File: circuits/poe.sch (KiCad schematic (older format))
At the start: 19 parts, among them U11 Si3402-B-GM(QFN-20_5x5mm)

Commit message: finished schematic corrections, working on layout
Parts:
- removed C11: C_100nF_1206, Capacitor_SMD:C_1206_3216Metric_Pad1.33x1.80mm_HandSolder, symbol Open_Automation:C_100nF_1206
- removed C12, C13: C_1uF_1206, Capacitor_SMD:C_1206_3216Metric_Pad1.33x1.80mm_HandSolder, symbol Open_Automation:C_1uF_1206
- removed C14: C_1nF_0402, Capacitor_SMD:C_0402_1005Metric_Pad0.74x0.62mm_HandSolder, symbol Open_Automation:C_1nF_0402
- removed C15: C_100nF_0402, Capacitor_SMD:C_0402_1005Metric_Pad0.74x0.62mm_HandSolder, symbol Open_Automation:C_100nF_0402
- removed C16: C_15uF, Capacitor_THT:CP_Radial_D6.3mm_P2.50mm, symbol Open_Automation:C_15uF
- removed C17: C_680uF, Capacitor_THT:CP_Radial_D6.3mm_P2.50mm, symbol Open_Automation:C_680uF
- removed C18: C_22uF_0805, Capacitor_SMD:C_0805_2012Metric_Pad1.18x1.45mm_HandSolder, symbol Open_Automation:C_22uF_0805
- removed D7: SS510, Diode_SMD:D_SMC_Handsoldering, symbol Open_Automation:SS510
- removed L1: L_33uH, Inductor_SMD:L_12x12mm_H6mm, symbol Open_Automation:L_33uH
- removed L2: FB, Inductor_SMD:L_1206_3216Metric, symbol Open_Automation:FB
- removed R46: R_47K_0402, Resistor_SMD:R_0402_1005Metric_Pad0.72x0.64mm_HandSolder, symbol Open_Automation:R_47K_0402
- removed R47: R_49.9_0402, Resistor_SMD:R_0402_1005Metric_Pad0.72x0.64mm_HandSolder, symbol Open_Automation:R_49.9_0402
- removed R48: R_25K5, Resistor_SMD:R_0603_1608Metric_Pad0.98x0.95mm_HandSolder, symbol Open_Automation:R_25K5
- removed R49: R_1K_0402, Resistor_SMD:R_0402_1005Metric_Pad0.72x0.64mm_HandSolder, symbol Open_Automation:R_1K_0402
- removed R50: R_8K2_0402, Resistor_SMD:R_0402_1005Metric_Pad0.72x0.64mm_HandSolder, symbol Open_Automation:R_8K2_0402
- removed SJ1, SJ2: SJ, Open_Automation:SJUMP, symbol Open_Automation:SJ
- removed U11: Si3402-B-GM(QFN-20_5x5mm), Open_Automation:QFN-20_5x5mm(Si3402-B-GM), symbol ESP32-PoE_Rev_E:Si3402-B-GM(QFN-20_5x5mm)
- added C11: C_2.2nF, Capacitor_SMD:C_1206_3216Metric_Pad1.33x1.80mm_HandSolder, symbol Open_Automation:C_2.2nF
- added C12: C_100nF_1206, Capacitor_SMD:C_1206_3216Metric_Pad1.33x1.80mm_HandSolder, symbol Open_Automation:C_100nF_1206
- added C13: C_0.1uF, Capacitor_SMD:C_0603_1608Metric_Pad1.08x0.95mm_HandSolder, symbol Open_Automation:C_0.1uF
- added C14: C_10nF, Capacitor_SMD:C_1206_3216Metric_Pad1.33x1.80mm_HandSolder, symbol Open_Automation:C_10nF
- added C15: C_47nF, Capacitor_SMD:C_0603_1608Metric_Pad1.08x0.95mm_HandSolder, symbol Open_Automation:C_47nF
- added C16: C_22uF_63V, Capacitor_SMD:C_Elec_6.3x7.7, symbol Open_Automation:C_22uF_63V
- added C17: C_220nF, Capacitor_SMD:C_1206_3216Metric_Pad1.33x1.80mm_HandSolder, symbol Open_Automation:C_220nF
- added C18: C_1uF_1206, Capacitor_SMD:C_1206_3216Metric_Pad1.33x1.80mm_HandSolder, symbol Open_Automation:C_1uF_1206
- added C19: C_10uF_Ta, Capacitor_Tantalum_SMD:CP_EIA-6032-15_Kemet-U_Pad2.25x2.35mm_HandSolder, symbol Open_Automation:C_10uF_Ta
- added C20: C_1uF, Capacitor_SMD:C_0603_1608Metric_Pad1.08x0.95mm_HandSolder, symbol Open_Automation:C_1uF
- added C21: C_47uF_Al, Capacitor_SMD:CP_Elec_6.3x7.7, symbol Open_Automation:C_47uF_Al
- added C22: C_100pF, Capacitor_SMD:C_0402_1005Metric_Pad0.74x0.62mm_HandSolder, symbol Open_Automation:C_100pF
- added C23: C_6.8nF, Capacitor_SMD:C_0402_1005Metric_Pad0.74x0.62mm_HandSolder, symbol Open_Automation:C_6.8nF
- added C24: C_47uF_Ta, Capacitor_Tantalum_SMD:CP_EIA-6032-15_Kemet-U_Pad2.25x2.35mm_HandSolder, symbol Open_Automation:C_47uF_Ta
- added C25: C_47uF, Capacitor_SMD:C_1210_3225Metric_Pad1.33x2.70mm_HandSolder, symbol Open_Automation:C_47uF
- added D10, D9: D_Bridge_+-AA, Open_Automation:Diode_Bridge_HD01, symbol Open_Automation:D_Bridge_+-AA
- added D11: D_SMAJ58A, Diode_SMD:D_SMA_Handsoldering, symbol Open_Automation:D_SMAJ58A
- added D12, D8: D_MURA120, Diode_SMD:D_SMA_Handsoldering, symbol Open_Automation:D_MURA120
- added D13, D14: BAS16, Package_TO_SOT_SMD:SOT-23, symbol Open_Automation:BAS16
- added D15: D_MBRS540T3G, Diode_SMD:D_SMC_Handsoldering, symbol Open_Automation:D_MBRS540T3G
- added J20: Conn_02x02_Counter_Clockwise, Connector_PinHeader_2.54mm:PinHeader_2x02_P2.54mm_Vertical_SMD, symbol Connector_Generic:Conn_02x02_Counter_Clockwise
- added L1: L_4.7uH, Open_Automation:L_5.4x5.3_H3, symbol Open_Automation:L_4.7uH
- added Q8: Q_FDC2512, Package_TO_SOT_SMD:SOT-23-6_Handsoldering, symbol Open_Automation:Q_FDC2512
- added R47: R_3.01K, Resistor_SMD:R_0603_1608Metric_Pad0.98x0.95mm_HandSolder, symbol Open_Automation:R_3.01K
- added R48: R_69.8K, Resistor_SMD:R_0603_1608Metric_Pad0.98x0.95mm_HandSolder, symbol Open_Automation:R_69.8K
- added R49: R_24.9K, Resistor_SMD:R_0603_1608Metric_Pad0.98x0.95mm_HandSolder, symbol Open_Automation:R_24.9K
- added R50: R_63.4, Resistor_SMD:R_0603_1608Metric_Pad0.98x0.95mm_HandSolder, symbol Open_Automation:R_63.4
- added R51: R_80.6K, Resistor_SMD:R_0402_1005Metric_Pad0.72x0.64mm_HandSolder, symbol Open_Automation:R_80.6K
- added R52: R_59K, Resistor_SMD:R_0402_1005Metric_Pad0.72x0.64mm_HandSolder, symbol Open_Automation:R_59K
- added R53, R60: R_49.9_0402, Resistor_SMD:R_0402_1005Metric_Pad0.72x0.64mm_HandSolder, symbol Open_Automation:R_49.9_0402
- added R54: R_49.9K, Resistor_SMD:R_0402_1005Metric_Pad0.72x0.64mm_HandSolder, symbol Open_Automation:R_49.9K
- added R55: R_0.56, Resistor_SMD:R_0603_1608Metric_Pad0.98x0.95mm_HandSolder, symbol Open_Automation:R_0.56
- added R56, R58: R_402, Resistor_SMD:R_0402_1005Metric_Pad0.72x0.64mm_HandSolder, symbol Open_Automation:R_402
- added R57: R_2K, Resistor_SMD:R_0402_1005Metric_Pad0.72x0.64mm_HandSolder, symbol Open_Automation:R_2K
- added R59: R_10K_0402, Resistor_SMD:R_0402_1005Metric_Pad0.72x0.64mm_HandSolder, symbol Open_Automation:R_10K_0402
- added R61: R_7.15K, Resistor_SMD:R_0402_1005Metric_Pad0.72x0.64mm_HandSolder, symbol Open_Automation:R_7.15K
- added R62: R_41.2K, Resistor_SMD:R_0402_1005Metric_Pad0.72x0.64mm_HandSolder, symbol Open_Automation:R_41.2K
- added R63: R_13.3K, Resistor_SMD:R_0402_1005Metric_Pad0.72x0.64mm_HandSolder, symbol Open_Automation:R_13.3K
- added TR1: TPS23754-TRANSFORMER, Open_Automation:TPS23754, symbol Open_Automation:TPS23754-TRANSFORMER
- added U11: TPS23754PWP-1, TPS23753:TPS23754PWP-1, symbol Open_Automation:TPS23754PWP-1
- added U12: OPTO-FOD817A, Open_Automation:Opto_FOD817A3SD, symbol Open_Automation:OPTO-FOD817A
- added U13: TLV431ACDBZR, Package_TO_SOT_SMD:SOT-23, symbol Open_Automation:TLV431ACDBZR
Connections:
- net labels added: APD, ARTN, BLNK, B_POS, CLS, COM, CS, CTL, DEN, DT, EPAD, FRS, GAT2, GATE, IN, PPD, T2P, TP1_N, TP1_P, VB, VC, VDC1+, VDC1-, VDC2+, VDC2-, VDD, VSS
- net labels removed: SP1, SP2, Spare1, Spare2
- wire segments 78 -> 155
- no-connect marks 2 -> 0
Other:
- note removed: "250mW(50mA@5V) minimal power consumption \non the PD required for to Maintain Power Signature(MPS)!"
- note removed: "CDET"
- note removed: "Class=0 (0.44 to 12.95W)"
- note removed: "PoE Power Supply"
- note removed: "RDET"
- note removed: "Ra"
- note removed: "Rb"
- note removed: "Rclass"
- note removed: "The Input filter capacitor must be >5 μF for to MPS!"
- note removed: "VOUT=1.35*(1+Ra/Rb)"
- note removed: "Vneg"
- note removed: "Vpos"
- note removed: "Vss"

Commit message: finished layout, sent to board house
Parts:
- removed J20: Conn_02x02_Counter_Clockwise, Connector_PinHeader_2.54mm:PinHeader_2x02_P2.54mm_Vertical_SMD, symbol Connector_Generic:Conn_02x02_Counter_Clockwise
- added J19: Conn_02x02_Odd_Even, Connector_PinHeader_2.54mm:PinHeader_2x02_P2.54mm_Vertical_SMD, symbol Connector_Generic:Conn_02x02_Odd_Even
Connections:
- net labels removed: ARTN, B_POS, COM, EPAD
- wire segments 155 -> 157
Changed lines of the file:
@@
-$EndComp
-$Comp
-L Open_Automation:TPS23754-TRANSFORMER TR1
-U 1 1 6042E6B6
-P 9200 3250
-F 0 "TR1" H 9200 3775 50  0000 C CNN
-F 1 "TPS23754-TRANSFORMER" H 9200 3684 50  0000 C CNN
-F 2 "Open_Automation:TPS23754" H 9200 3250 50  0001 C CNN
-F 3 "https://www.coilcraft.com/getmedia/82697be8-7a7c-4b54-a33e-3e538a882584/ja4372.pdf" H 9200 3250 50  0001 C CNN
-F 4 "JA4387-AL" H 9200 2550 50  0001 C CNN "Part Number"
-	1    9200 3250
-	1    0    0    -1
 $EndComp
 $Comp
@@
 Text Label 3900 3500 2    50   ~ 0
 BLNK
-Text Label 3900 3800 2    50   ~ 0
-EPAD
 Text Label 3900 3100 2    50   ~ 0
 PPD
@@
 Text Label 3900 3300 2    50   ~ 0
 DT
-Text Label 5550 3050 0    50   ~ 0
-ARTN
 Text Label 5550 3250 0    50   ~ 0
 VC
@@
 Text Label 5550 3550 0    50   ~ 0
 CS
-Text Label 5550 3450 0    50   ~ 0
-COM
 Text Label 5550 3750 0    50   ~ 0
 CTL
@@
 Wire Wire Line
 	5500 3050 5550 3050
-Wire Wire Line
-	5550 2950 5500 2950
 Wire Wire Line
 	5550 2850 5500 2850
@@
 L power:Earth #PWR089
 U 1 1 605ECE0C
-P 5550 2950
+P 5600 2950
 AR Path="/60124B38/605ECE0C" Ref="#PWR089"  Part="1"
 AR Path="/603C306C/605ECE0C" Ref="#PWR?"  Part="1"
-F 0 "#PWR089" H 5550 2700 50  0001 C CNN
-F 1 "Earth" H 5550 2800 50  0001 C CNN
-F 2 "" H 5550 2950 50  0001 C CNN
-F 3 "~" H 5550 2950 50  0001 C CNN
-	1    5550 2950
+F 0 "#PWR089" H 5600 2700 50  0001 C CNN
+F 1 "Earth" H 5600 2800 50  0001 C CNN
+F 2 "" H 5600 2950 50  0001 C CNN
+F 3 "~" H 5600 2950 50  0001 C CNN
+	1    5600 2950
 	0    -1   -1   0
 $EndComp
@@
 Wire Wire Line
 	2750 2850 2700 2850
-Text Label 3100 2850 0    50   ~ 0
-B_POS
 Wire Wire Line
 	3100 2850 3050 2850
@@
 	1300 3400 1100 3400
 Connection ~ 1100 3400
-$Comp
-L Connector_Generic:Conn_02x02_Counter_Clockwise J20
-U 1 1 6073A3C4
-P 1150 2450
-F 0 "J20" H 1200 2667 50  0000 C CNN
-F 1 "Conn_02x02_Counter_Clockwise" H 1200 2576 50  0000 C CNN
-F 2 "Connector_PinHeader_2.54mm:PinHeader_2x02_P2.54mm_Vertical_SMD" H 1150 2450 50  0001 C CNN
-F 3 "~" H 1150 2450 50  0001 C CNN
-	1    1150 2450
-	1    0    0    -1
-$EndComp
 $Comp
 L power:Earth #PWR085
@@
 	1    0    0    -1
 $EndComp
+$Comp
+L Connector_Generic:Conn_02x02_Odd_Even J19
+U 1 1 6242130D
+P 1150 2450
+F 0 "J19" H 1200 2667 50  0000 C CNN
+F 1 "Conn_02x02_Odd_Even" H 1200 2576 50  0000 C CNN
+F 2 "Connector_PinHeader_2.54mm:PinHeader_2x02_P2.54mm_Vertical_SMD" H 1150 2450 50  0001 C CNN
+F 3 "~" H 1150 2450 50  0001 C CNN
+	1    1150 2450
+	1    0    0    -1
+$EndComp
+$Comp
+L Open_Automation:TPS23754-TRANSFORMER TR1
+U 1 1 6042E6B6
+P 9200 3250
+F 0 "TR1" H 9200 3775 50  0000 C CNN
+F 1 "TPS23754-TRANSFORMER" H 9200 3684 50  0000 C CNN
+F 2 "Open_Automation:TPS23754" H 9200 3250 50  0001 C CNN
+F 3 "https://www.coilcraft.com/getmedia/82697be8-7a7c-4b54-a33e-3e538a882584/ja4372.pdf" H 9200 3250 50  0001 C CNN
+F 4 "JA4387-AL" H 9200 2550 50  0001 C CNN "Part Number"
+	1    9200 3250
+	1    0    0    -1
+$EndComp
+Text Label 3100 2850 0    50   ~ 0
+VDD
+Text Label 3900 3800 2    50   ~ 0
+VSS
+Wire Wire Line
+	5500 2950 5550 2950
+Wire Wire Line
+	5550 3050 5550 2950
+Connection ~ 5550 2950
+Wire Wire Line
+	5550 2950 5600 2950
+$Comp
+L power:Earth #PWR?
+U 1 1 6275A8E7
+P 5550 3450
+AR Path="/60124B38/6275A8E7" Ref="#PWR?"  Part="1"
+AR Path="/603C306C/6275A8E7" Ref="#PWR?"  Part="1"
+F 0 "#PWR?" H 5550 3200 50  0001 C CNN
+F 1 "Earth" H 5550 3300 50  0001 C CNN
+F 2 "" H 5550 3450 50  0001 C CNN
+F 3 "~" H 5550 3450 50  0001 C CNN
+	1    5550 3450
+	0    -1   -1   0
+$EndComp
 $EndSCHEMATC

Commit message: got board back from fab, testing
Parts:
- C13: footprint Capacitor_SMD:C_0603_1608Metric_Pad1.08x0.95mm_HandSolder -> Capacitor_SMD:C_0402_1005Metric_Pad0.74x0.62mm_HandSolder; LCSC C14663 -> C1525; Part Number CC0603KRX7R9BB104 -> CL05B104KO5NNNC
- C14: footprint Capacitor_SMD:C_1206_3216Metric_Pad1.33x1.80mm_HandSolder -> Capacitor_SMD:C_0805_2012Metric_Pad1.18x1.45mm_HandSolder
- C20: footprint Capacitor_SMD:C_0603_1608Metric_Pad1.08x0.95mm_HandSolder -> Capacitor_SMD:C_0402_1005Metric_Pad0.74x0.62mm_HandSolder
- U11: LCSC C202179 -> C181651
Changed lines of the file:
@@
 F 3 "https://www.ti.com/lit/gpn/tps23754" H 5500 3750 60  0001 C CNN
 F 4 "TPS23754PWPR" H 5500 3750 50  0001 C CNN "Part Number"
-F 5 "C202179" H 5500 3750 50  0001 C CNN "LCSC"
+F 5 "C181651" H 5500 3750 50  0001 C CNN "LCSC"
 	1    5500 3750
 	-1   0    0    1
@@
 F 0 "C14" H 7265 2746 50  0000 L CNN
 F 1 "C_10nF" H 7265 2655 50  0000 L CNN
-F 2 "Capacitor_SMD:C_1206_3216Metric_Pad1.33x1.80mm_HandSolder" H 7250 3000 50  0001 C CNN
+F 2 "Capacitor_SMD:C_0805_2012Metric_Pad1.18x1.45mm_HandSolder" H 7250 3000 50  0001 C CNN
 F 3 "https://datasheet.lcsc.com/szlcsc/Samsung-Electro-Mechanics-CL21B103KCANNNC_C18741.pdf" H 7150 2450 50  0001 C CNN
 F 4 "C18741" H 7150 3100 50  0001 C CNN "LCSC"
@@
 F 0 "C13" H 6650 5000 50  0000 L CNN
 F 1 "C_0.1uF" H 6550 4900 50  0000 L CNN
-F 2 "Capacitor_SMD:C_0603_1608Metric_Pad1.08x0.95mm_HandSolder" H 6950 5300 50  0001 C CNN
-F 3 "https://datasheet.lcsc.com/szlcsc/YAGEO-CC0603KRX7R9BB104_C14663.pdf" H 6850 4750 50  0001 C CNN
-F 4 "CC0603KRX7R9BB104" H 6975 5200 60  0001 C CNN "Part Number"
-F 5 "C14663" H 6850 5400 50  0001 C CNN "LCSC"
+F 2 "Capacitor_SMD:C_0402_1005Metric_Pad0.74x0.62mm_HandSolder" H 6950 5300 50  0001 C CNN
+F 3 "https://datasheet.lcsc.com/szlcsc/Samsung-Electro-Mechanics-CL05B104KO5NNNC_C1525.pdf" H 6850 4750 50  0001 C CNN
+F 4 "CL05B104KO5NNNC" H 6975 5200 60  0001 C CNN "Part Number"
+F 5 "C1525" H 6850 5400 50  0001 C CNN "LCSC"
 	1    6850 5000
 	1    0    0    -1
@@
 F 0 "C20" H 8400 6000 50  0000 L CNN
 F 1 "C_1uF" H 8350 5900 50  0000 L CNN
-F 2 "Capacitor_SMD:C_0603_1608Metric_Pad1.08x0.95mm_HandSolder" H 8700 6300 50  0001 C CNN
+F 2 "Capacitor_SMD:C_0402_1005Metric_Pad0.74x0.62mm_HandSolder" H 8700 6300 50  0001 C CNN
 F 3 "https://datasheet.lcsc.com/szlcsc/Samsung-Electro-Mechanics-CL05A105KA5NQNC_C52923.pdf" H 8600 5750 50  0001 C CNN
 F 4 "C52923" H 8600 6400 50  0001 C CNN "LCSC"

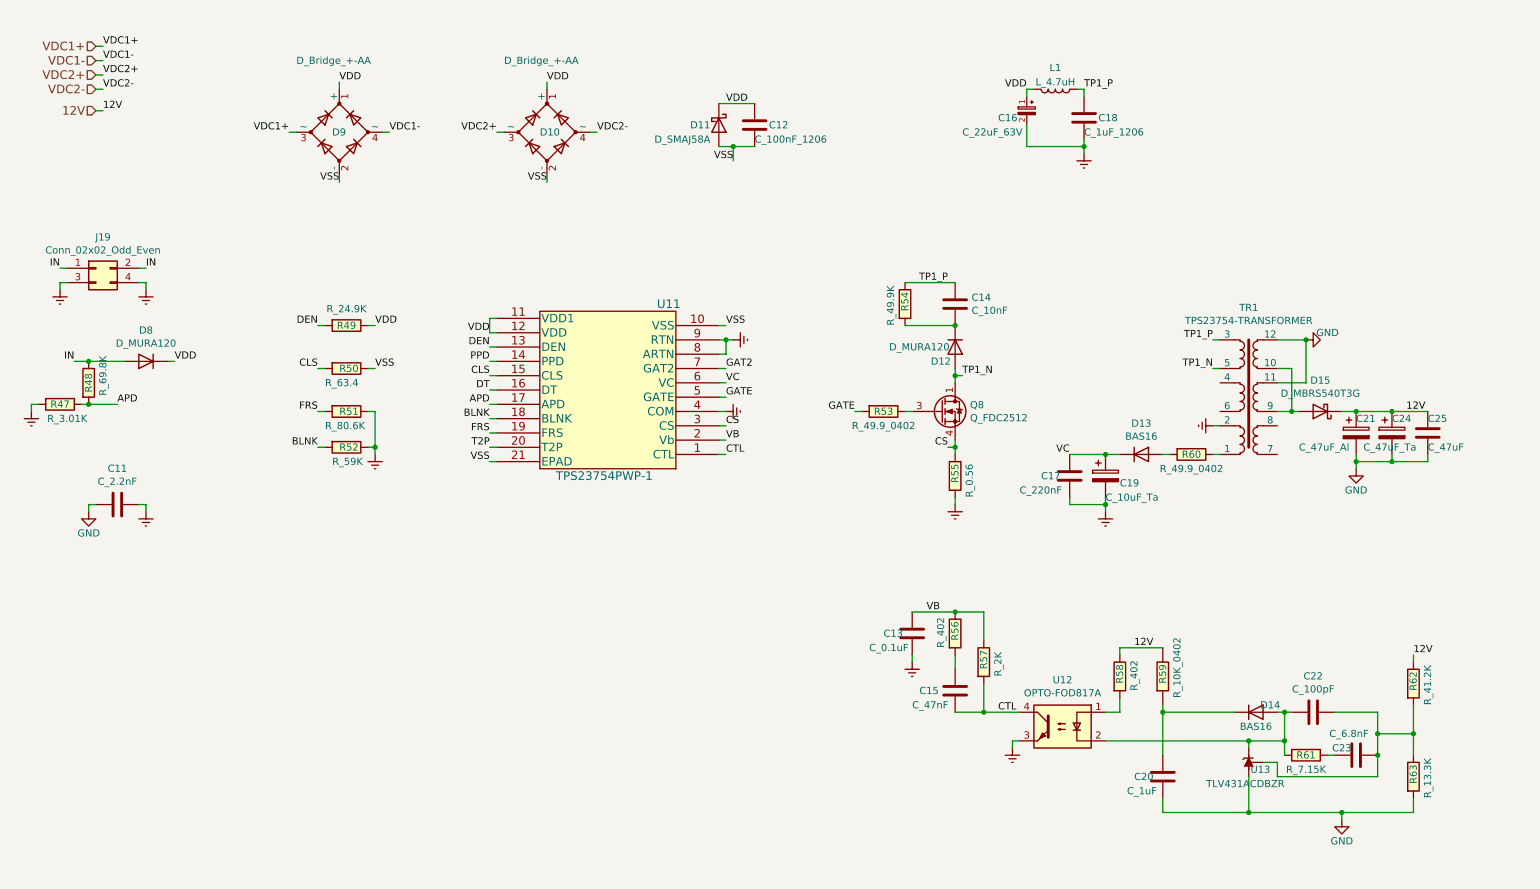
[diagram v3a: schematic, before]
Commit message: modifed PoE circuit
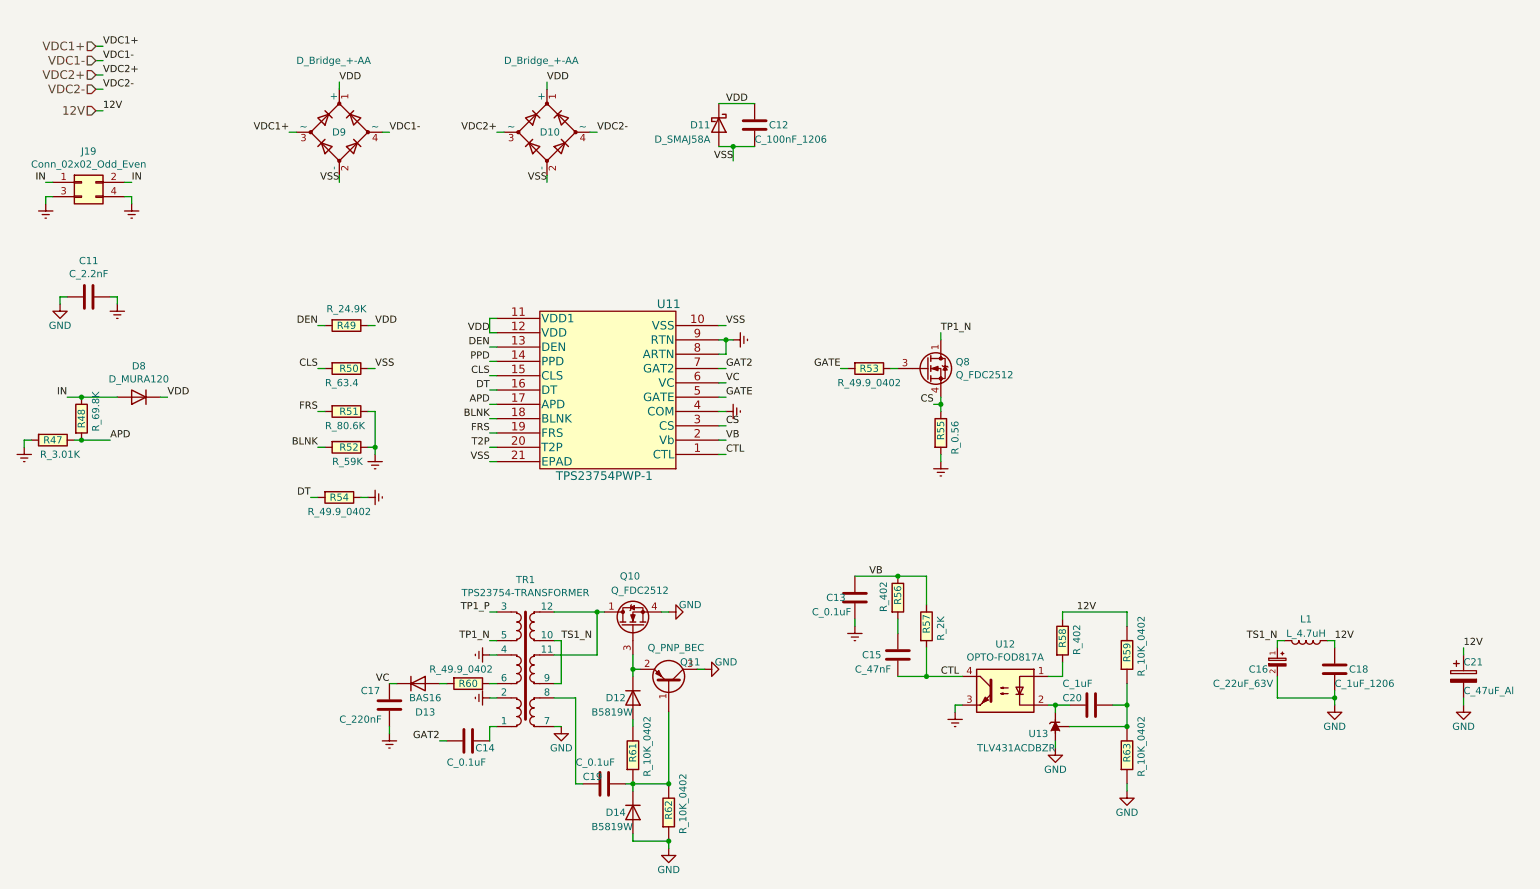
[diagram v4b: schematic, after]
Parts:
- removed C14: C_10nF, Capacitor_SMD:C_0805_2012Metric_Pad1.18x1.45mm_HandSolder, symbol Open_Automation:C_10nF
- removed C19: C_10uF_Ta, Capacitor_Tantalum_SMD:CP_EIA-6032-15_Kemet-U_Pad2.25x2.35mm_HandSolder, symbol Open_Automation:C_10uF_Ta
- removed C22: C_100pF, Capacitor_SMD:C_0402_1005Metric_Pad0.74x0.62mm_HandSolder, symbol Open_Automation:C_100pF
- removed C23: C_6.8nF, Capacitor_SMD:C_0402_1005Metric_Pad0.74x0.62mm_HandSolder, symbol Open_Automation:C_6.8nF
- removed C24: C_47uF_Ta, Capacitor_Tantalum_SMD:CP_EIA-6032-15_Kemet-U_Pad2.25x2.35mm_HandSolder, symbol Open_Automation:C_47uF_Ta
- removed C25: C_47uF, Capacitor_SMD:C_1210_3225Metric_Pad1.33x2.70mm_HandSolder, symbol Open_Automation:C_47uF
- removed D12: D_MURA120, Diode_SMD:D_SMA_Handsoldering, symbol Open_Automation:D_MURA120
- removed D14: BAS16, Package_TO_SOT_SMD:SOT-23, symbol Open_Automation:BAS16
- removed D15: D_MBRS540T3G, Diode_SMD:D_SMC_Handsoldering, symbol Open_Automation:D_MBRS540T3G
- removed R54: R_49.9K, Resistor_SMD:R_0402_1005Metric_Pad0.72x0.64mm_HandSolder, symbol Open_Automation:R_49.9K
- removed R61: R_7.15K, Resistor_SMD:R_0402_1005Metric_Pad0.72x0.64mm_HandSolder, symbol Open_Automation:R_7.15K
- removed R62: R_41.2K, Resistor_SMD:R_0402_1005Metric_Pad0.72x0.64mm_HandSolder, symbol Open_Automation:R_41.2K
- removed R63: R_13.3K, Resistor_SMD:R_0402_1005Metric_Pad0.72x0.64mm_HandSolder, symbol Open_Automation:R_13.3K
- added C14, C19: C_0.1uF, Capacitor_SMD:C_0402_1005Metric_Pad0.74x0.62mm_HandSolder, symbol Open_Automation:C_0.1uF
- added D12, D14: B5819W, Diode_SMD:D_SOD-123, symbol Open_Automation:B5819W
- added Q10: Q_FDC2512, Package_TO_SOT_SMD:SOT-23-6_Handsoldering, symbol Open_Automation:Q_FDC2512
- added Q11: Q_PNP_BEC, Package_TO_SOT_SMD:SOT-23, symbol Open_Automation:Q_PNP_BEC
- added R54: R_49.9_0402, Resistor_SMD:R_0402_1005Metric_Pad0.72x0.64mm_HandSolder, symbol Open_Automation:R_49.9_0402
- added R61, R62, R63: R_10K_0402, Resistor_SMD:R_0402_1005Metric_Pad0.72x0.64mm_HandSolder, symbol Open_Automation:R_10K_0402
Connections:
- net 12V: now also C18.1, L1.1
- net DT: now also R54.2
- net Earth: now also TR1.4, R54.1; no longer C16.2 (-), C18.2
- net GAT2: now also C14.2
- net GND: now also C16.2 (-), C18.2, TR1.7, D14.2 (NC), Q10.4 (S), Q11.3 (C), R62.1, R63.1; no longer C20.2, TR1.11, TR1.12
- net TP1_P: no longer C18.1, L1.1
- net VDD: no longer C16.1 (+), L1.2
- net at TR1.1: now also C14.1; no longer R60.1
- net TS1_N: now reaches TR1.10, TR1.9
- net TS1_N: now also C16.1 (+), L1.2
- net at TR1.6: now also R60.1
- net at TR1.8: now also C19.2
- net at U12.2, U13.2 (K): now also C20.2
- net at C20.1, R59.1: now also U13.1 (REF), R63.2
- new net: Q10.1 (D), Q10.2 (D), Q10.5 (D), Q10.6 (D), TR1.11, TR1.12
- new net: D12.1 (K), Q10.3 (G), Q11.2 (E)
- new net: D12.2 (NC), R61.2
- new net: C19.1, D14.1 (K), Q11.1 (B), R61.1, R62.2
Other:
- moved on the sheet: C11, C13, C15, C16, C17, C18, C20, C21, D13, D8, J19, L1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
